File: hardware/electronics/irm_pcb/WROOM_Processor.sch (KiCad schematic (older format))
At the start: 6 parts, among them J17 Conn_01x06, J9 Conn_02x15_Top_Bottom, SW1 RST, SW2 0, U5 ESP32-WROOM-32

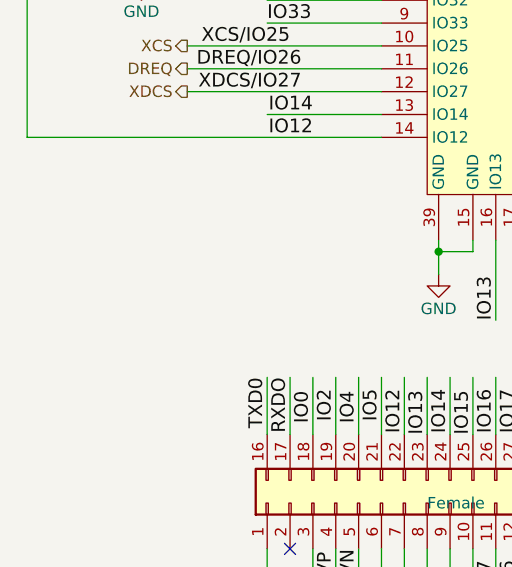
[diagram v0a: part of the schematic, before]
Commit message: Added WROOM decoupling capacitors
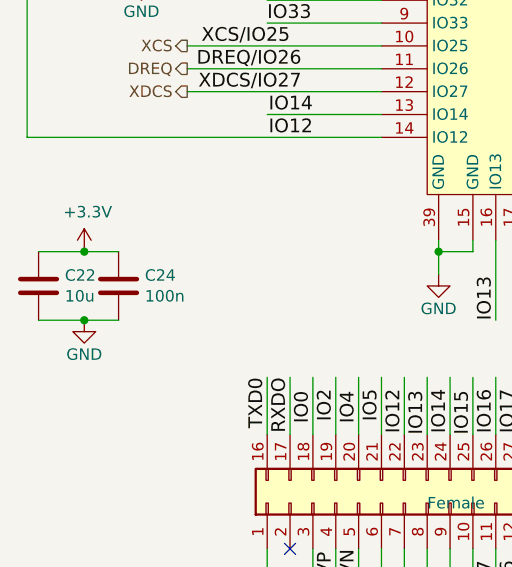
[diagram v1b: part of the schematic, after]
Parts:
- added C22: 10u, Capacitor_SMD:C_0805_2012Metric_Pad1.15x1.40mm_HandSolder, symbol Device:C
- added C24: 100n, Capacitor_SMD:C_0805_2012Metric_Pad1.15x1.40mm_HandSolder, symbol Device:C
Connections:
- wire segments 79 -> 83
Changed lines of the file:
@@
 RS
 Wire Wire Line
-	2600 3550 2600 1550
-Wire Wire Line
 	2600 1550 7100 1550
 Wire Wire Line
@@
 Wire Wire Line
 	7100 2100 7350 2100
-Wire Wire Line
-	2600 3550 4150 3550
 Text Notes 7250 3650 0    50   ~ 0
 -> LCD DRIVERS
@@
 Wire Notes Line
 	7800 4700 6600 4700
+Wire Wire Line
+	2850 4350 3000 4350
+Connection ~ 2850 4350
+$Comp
+L modular-internet-radio:GND #PWR?
+U 1 1 5DFD3A19
+P 2850 4350
+AR Path="/5DFD3A19" Ref="#PWR?"  Part="1"
+AR Path="/5DB85C19/5DFD3A19" Ref="#PWR0106"  Part="1"
+F 0 "#PWR0106" H 2850 4100 50  0001 C CNN
+F 1 "GND" H 2850 4200 50  0000 C CNN
+F 2 "" H 2850 4350 50  0000 C CNN
+F 3 "" H 2850 4350 50  0000 C CNN
+	1    2850 4350
+	1    0    0    -1
+$EndComp
+Wire Wire Line
+	2850 4050 3000 4050
+Connection ~ 2850 4050
+$Comp
+L modular-internet-radio:+3.3V #PWR?
+U 1 1 5DFD3465
+P 2850 4050
+AR Path="/5DFD3465" Ref="#PWR?"  Part="1"
+AR Path="/5DB85C19/5DFD3465" Ref="#PWR0107"  Part="1"
+F 0 "#PWR0107" H 2850 3900 50  0001 C CNN
+F 1 "+3.3V" H 2865 4223 50  0000 C CNN
+F 2 "" H 2850 4050 50  0000 C CNN
+F 3 "" H 2850 4050 50  0000 C CNN
+	1    2850 4050
+	1    0    0    -1
+$EndComp
+Wire Wire Line
+	2650 4350 2850 4350
+Wire Wire Line
+	2650 4050 2850 4050
+$Comp
+L Device:C C24
+U 1 1 5DFCEEB1
+P 3000 4200
+F 0 "C24" H 3115 4246 50  0000 L CNN
+F 1 "100n" H 3115 4155 50  0000 L CNN
+F 2 "Capacitor_SMD:C_0805_2012Metric_Pad1.15x1.40mm_HandSolder" H 3038 4050 50  0001 C CNN
+F 3 "~" H 3000 4200 50  0001 C CNN
+	1    3000 4200
+	1    0    0    -1
+$EndComp
+$Comp
+L Device:C C22
+U 1 1 5DFCEAA0
+P 2650 4200
+F 0 "C22" H 2765 4246 50  0000 L CNN
+F 1 "10u" H 2765 4155 50  0000 L CNN
+F 2 "Capacitor_SMD:C_0805_2012Metric_Pad1.15x1.40mm_HandSolder" H 2688 4050 50  0001 C CNN
+F 3 "~" H 2650 4200 50  0001 C CNN
+	1    2650 4200
+	1    0    0    -1
+$EndComp
+Wire Wire Line
+	2600 3550 4150 3550
+Wire Wire Line
+	2600 3550 2600 1550
 $EndSCHEMATC
